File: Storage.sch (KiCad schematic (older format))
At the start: 21 parts, among them J8 Micro_SD_Card_Det, U17 FTDITypeUART, U18 ABRACON-ASDMB, U19 S25FL256SAGNFI001, U20 xc7z020clg484

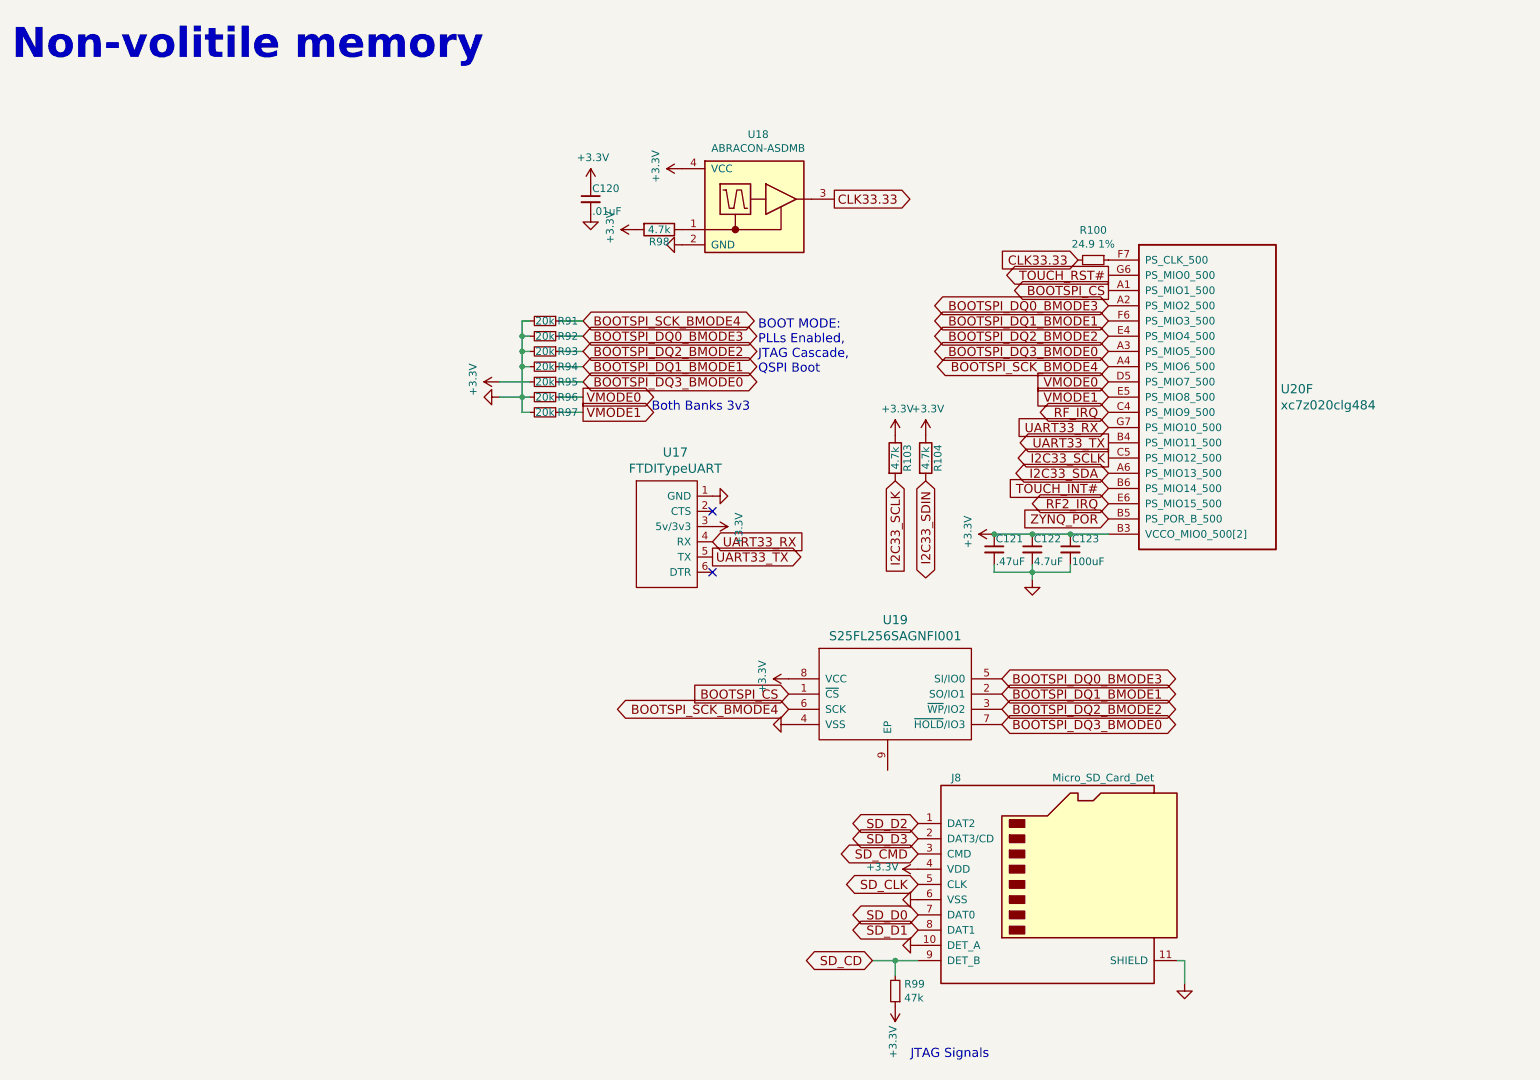
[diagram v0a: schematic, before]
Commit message: low 2 ddr3 bytes delay matched WRT package flight time
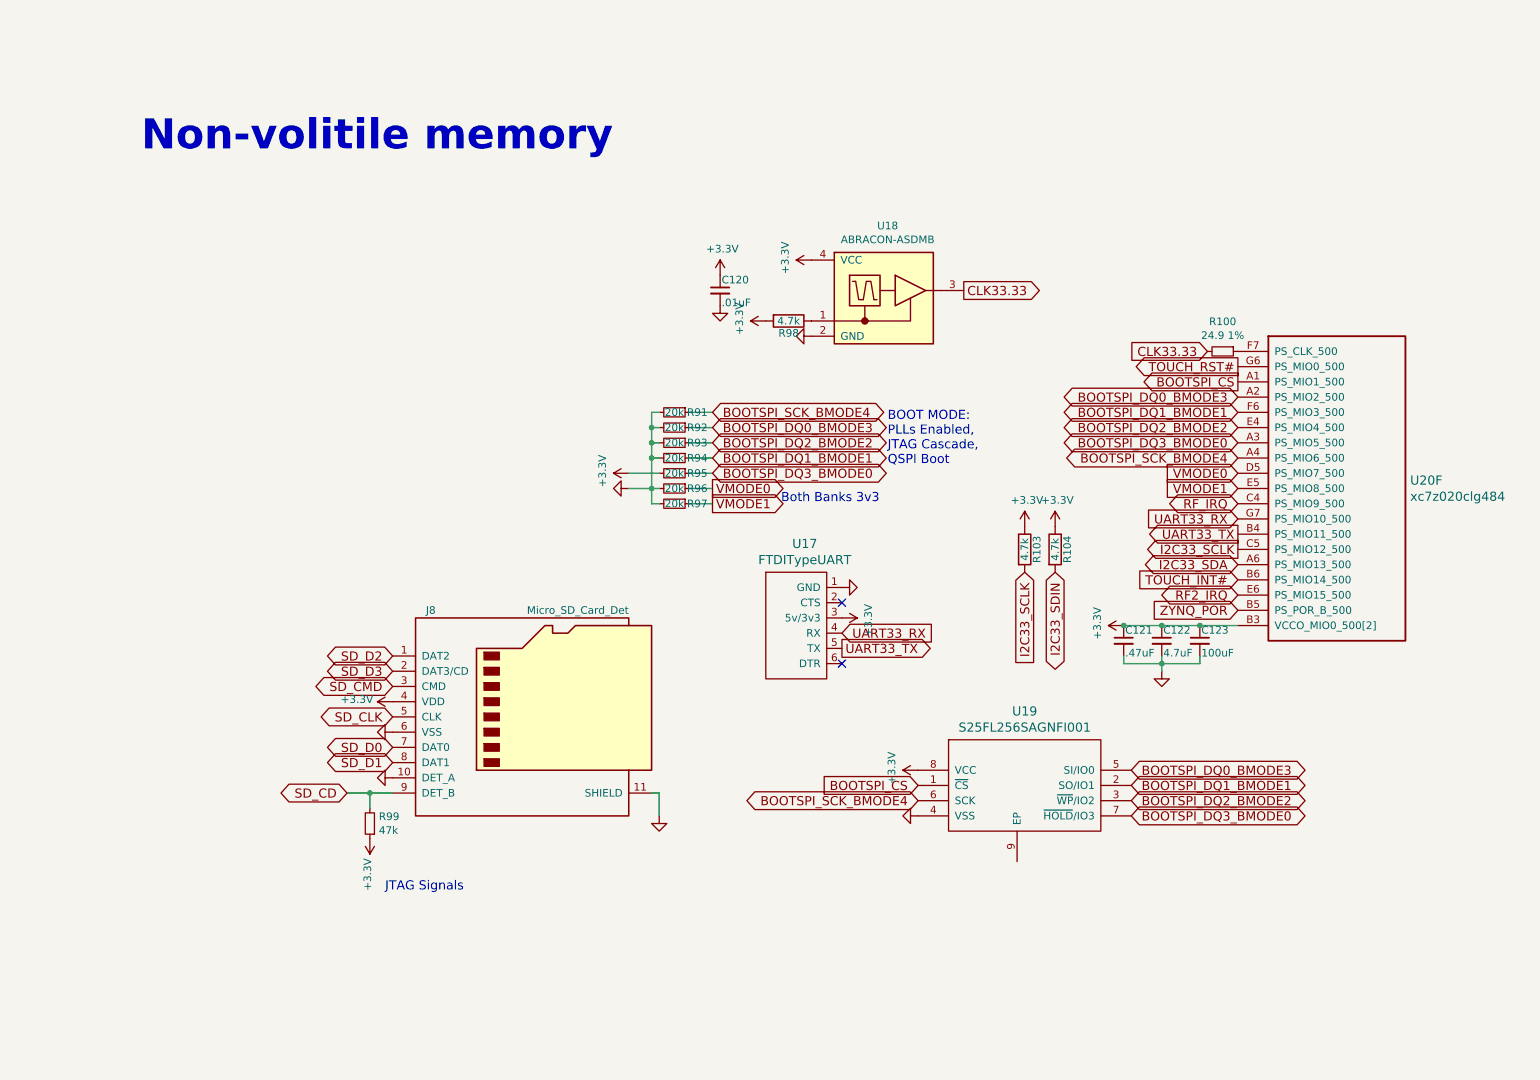
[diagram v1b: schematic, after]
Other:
- moved on the sheet: C120, C121, C122, C123, J8, R100, R103, R104, R91, R92, R93, R94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

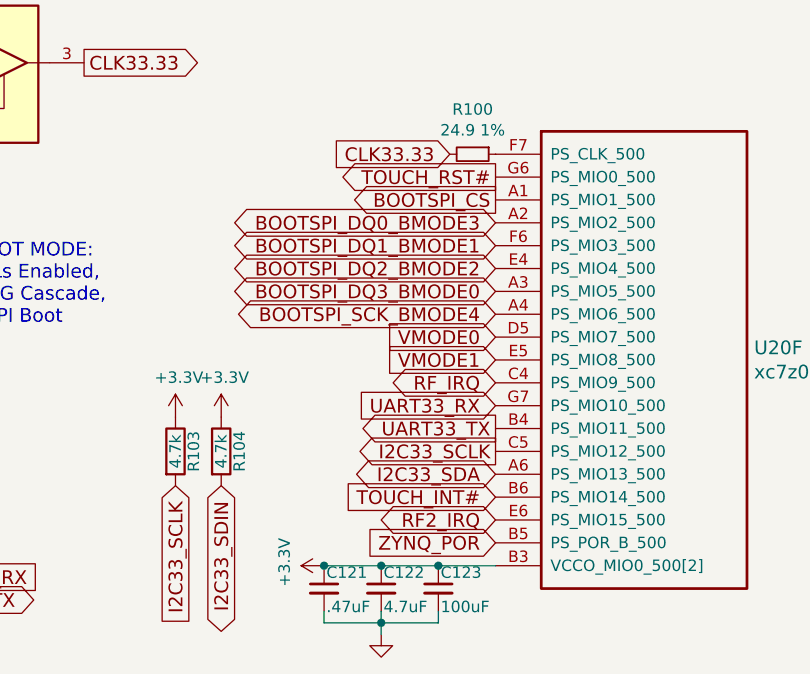
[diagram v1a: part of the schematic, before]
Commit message: routed a few things, about to remove power jack and 5V regulator
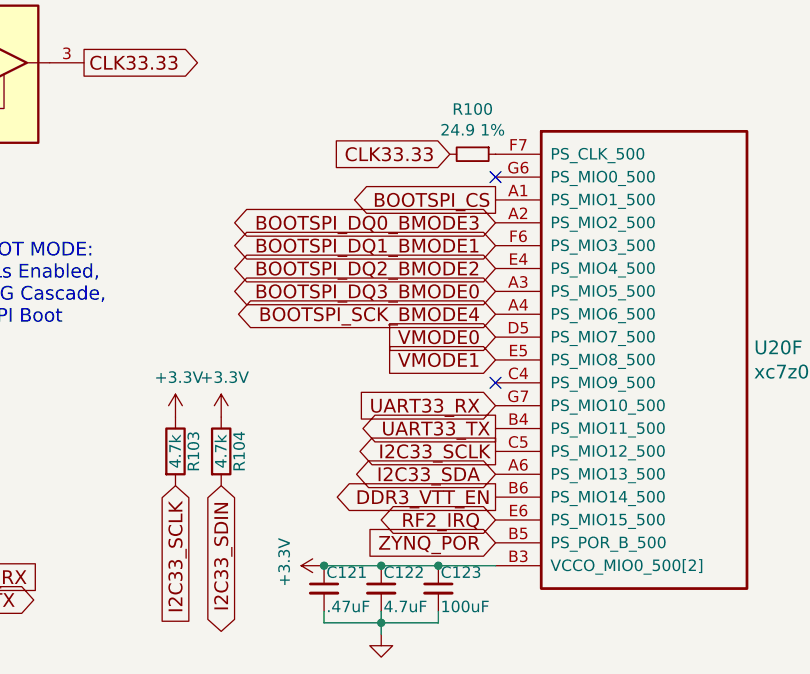
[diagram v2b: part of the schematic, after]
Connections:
- net RF_IRQ: no longer names the net of U20.C4 (PS_MIO9_500)
- net TOUCH_INT# renamed DDR3_VTT_EN
- net TOUCH_RST#: no longer names the net of U20.G6 (PS_MIO0_500)
- no-connect marks 2 -> 4
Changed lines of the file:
@@
 Text Notes 2550 6000 0    60   ~ 0
 JTAG Signals
-Text GLabel 8150 2550 0    60   Output ~ 0
-TOUCH_RST#
-Text GLabel 8150 3950 0    60   Input ~ 0
-TOUCH_INT#
 $Comp
 L DFTBoard-rescue:Micro_SD_Card_Det- J?
@@
 Wire Wire Line
 	4350 5350 4350 5500
-Text GLabel 8150 3450 0    60   BiDi ~ 0
-RF_IRQ
 $Comp
 L power:GND #PWR?
@@
 	1    0    0    -1
 $EndComp
+NoConn ~ 8150 2550
+NoConn ~ 8150 3450
+Text GLabel 8150 3950 0    60   Output ~ 0
+DDR3_VTT_EN
 $EndSCHEMATC

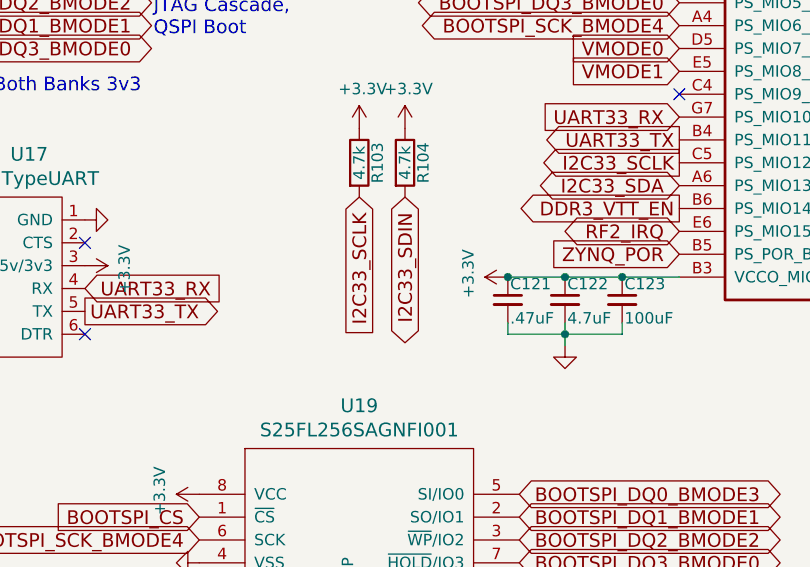
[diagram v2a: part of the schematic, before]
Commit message: downto 70 unrouted. moved SD interface back to MIO
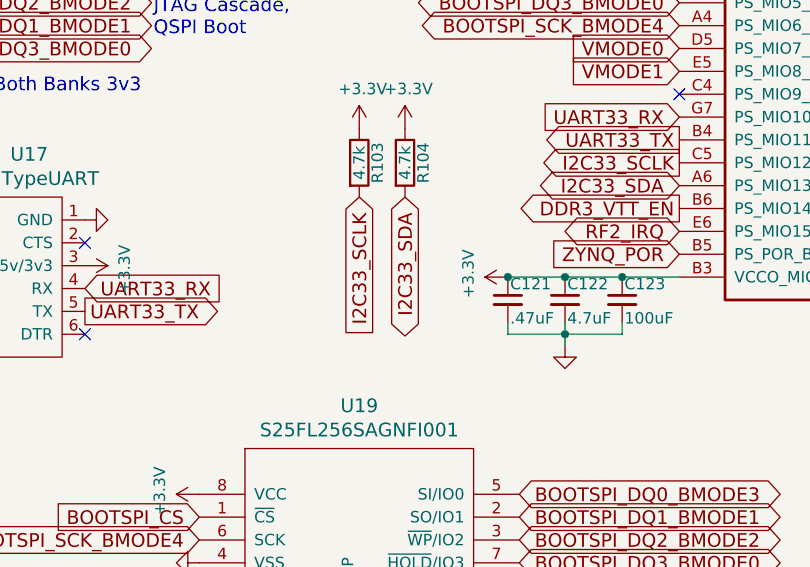
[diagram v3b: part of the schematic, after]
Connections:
- net I2C33_SDIN is gone; now on net I2C33_SDA: R104.2
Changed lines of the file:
@@
 I2C33_SCLK
 Text GLabel 6950 3900 3    60   BiDi ~ 0
-I2C33_SDIN
+I2C33_SDA
 $Comp
 L power:+3V3 #PWR?

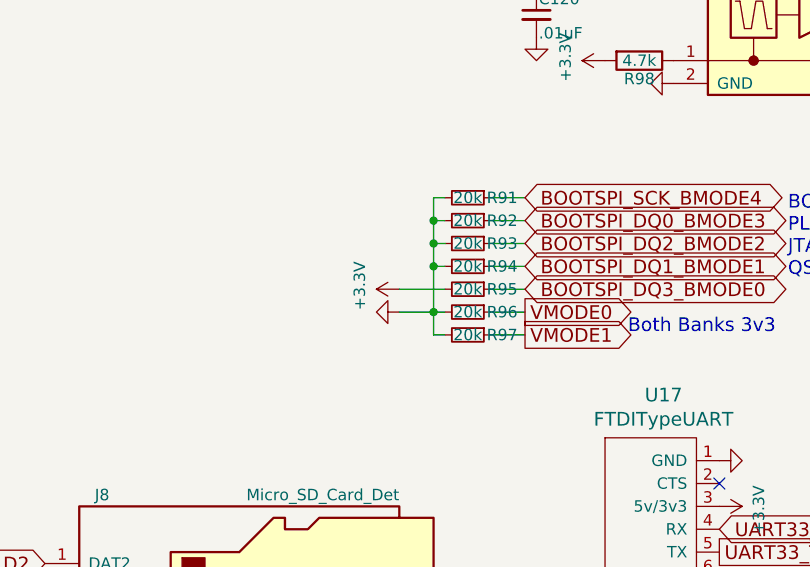
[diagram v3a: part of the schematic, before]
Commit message: length matched important interfaces, added current sense resistors to regulators, about to shrink silkscreen designators
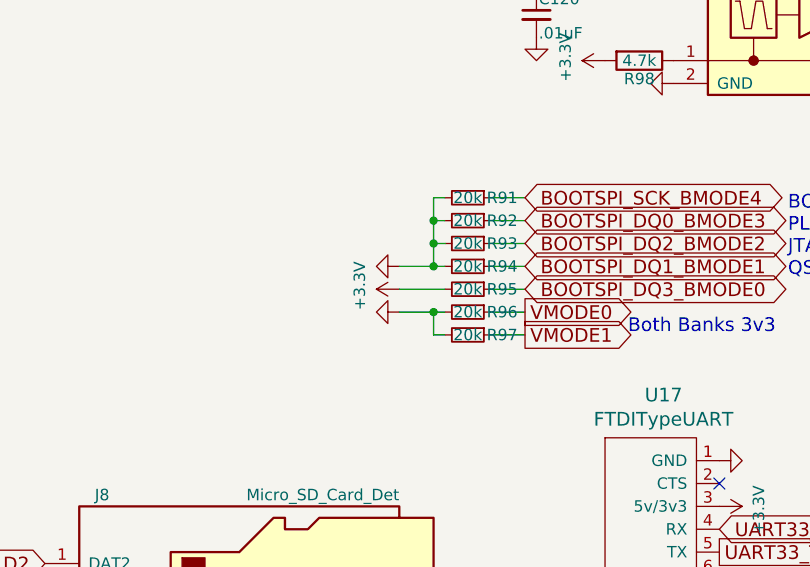
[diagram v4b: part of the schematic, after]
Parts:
- C120: MPN (none) -> GRM155R71H103KA88J; SPN (none) -> 490-6351-1-ND; SPURL (none) -> -
- J8: MFR (none) -> Amphenol ICC; MPN (none) -> 114-00841-68; SPN (none) -> 114-00841-68-1-ND; SPR (none) -> Digikey; SPURL (none) -> -
- R100: MFR (none) -> Yageo; MPN (none) -> RC0402FR-0724K9L; SPN (none) -> 311-24.9KLRTR-ND; SPR (none) -> Digikey; SPURL (none) -> -
- R103, R104, R98: MPN RC0402FR-074K7L -> RC0402JR-074K7L; SPN 311-4.7KLRCT-ND -> 311-4.7KJRCT-ND
- R91, R92, R93, R94, R95, R96, R97: MFR (none) -> Yageo; MPN (none) -> RT0402BRD0720KL; SPN (none) -> YAG1388CT-ND; SPR (none) -> Digikey; SPURL (none) -> -
- R99: MFR (none) -> Yageo; MPN (none) -> RC0402FR-0747KL; SPN (none) -> 311-47.0KLRTR-ND; SPR (none) -> Digikey; SPURL (none) -> -
- U17: MFR (none) -> DNS; MPN (none) -> -; SPN (none) -> -; SPR (none) -> -; SPURL (none) -> -
- U18: MFR (none) -> Abracon LLC; MPN ASDMB-{freq}MHZ-{temp}{stab}-{load}-{pkg} -> ASDMB-24.000MHZ-LC-T; SPN (none) -> 535-11728-1-ND; SPR (none) -> Digikey; SPURL (none) -> -
- U19: MFR (none) -> Cypress; MPN (none) -> S25FL256SAGNFI001; SPN (none) -> 1274-1005-ND; SPR (none) -> Digikey; SPURL (none) -> -
- U20: MFR (none) -> Xilinx; MPN (none) -> XC7Z020-1CLG484C; SPN (none) -> 122-1850-ND; SPR (none) -> Digikey; SPURL (none) -> -

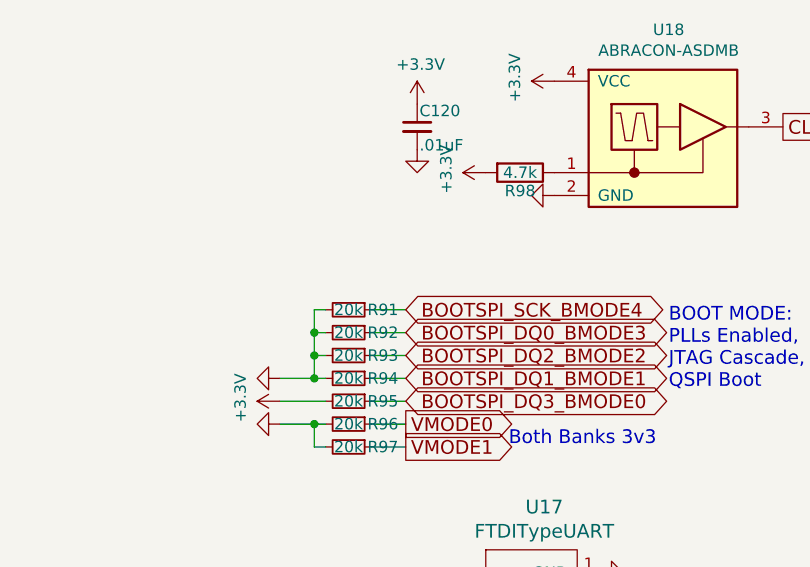
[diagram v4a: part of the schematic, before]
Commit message: finished review with gerber output. still need to relocate rangefinders / LEDs
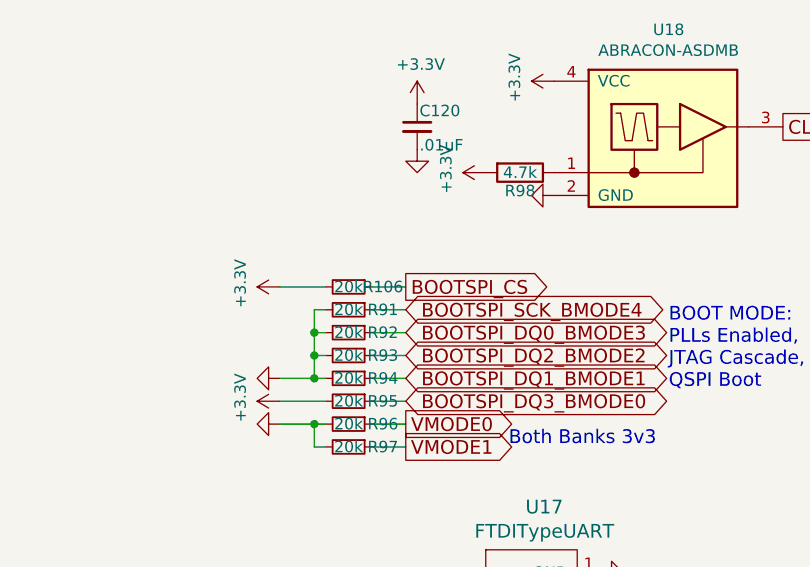
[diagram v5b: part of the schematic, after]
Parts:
- added R106: 20k, Resistor_SMD:R_0402_1005Metric, symbol Device:R_Small
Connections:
- net +3V3: now also R106.2
- net BOOTSPI_CS: now also R106.1

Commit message: some part changes for BOM clarification
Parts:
- C121: MFR Murata -> Yageo; MPN GRM188R71C474KA88D -> CC0402KRX5R5BB474; SPN 490-3295-1-ND -> 311-1684-1-ND
- C122: MPN GRM21BR61A475KA73L -> GRM155R60G475ME47D; SPN 490-9750-1-ND -> 490-11980-1-ND
